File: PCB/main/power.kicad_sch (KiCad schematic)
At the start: 13 parts, among them J2 PH2 protected pack, U4 AP2112K-3.3TRG1, U6 BQ24074RGTR

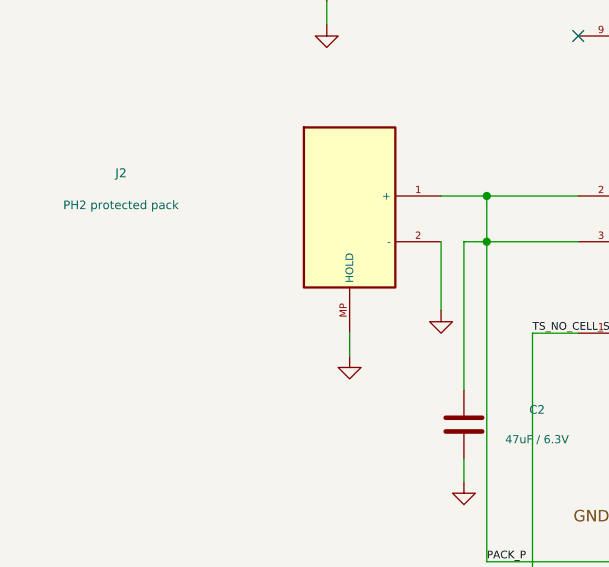
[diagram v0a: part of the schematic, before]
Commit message: Compact PCB and housing with 2.54mm PTH battery wire pads
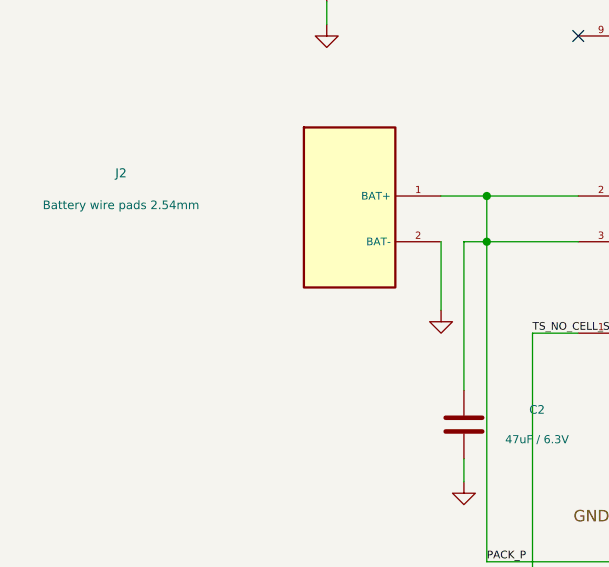
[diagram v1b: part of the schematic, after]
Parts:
- J2: value PH2 protected pack -> Battery wire pads 2.54mm; footprint smove-r2-main:JST_PH_S2B-PH-SM4-TB_1x02-1MP_P2.00mm_Horizontal -> smove-r2-main:BatteryWire_2x_PTH_P2.54mm_D1.0mm; LCSC C295747 -> (none); MPN S2B-PH-SM4-TB(LF)(SN) -> (none); now left out of the parts list
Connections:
- net GND: no longer J2.MP (HOLD)
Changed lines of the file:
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@@
     (at 50.8 77.47 0)
     (unit 1)
-    (in_bom yes)
+    (in_bom no)
     (on_board yes)
     (dnp no)
@@
         (font
           (size 1 1))))
-    (property "Value" "PH2 protected pack"
+    (property "Value" "Battery wire pads 2.54mm"
       (at 25.4 77.216 0)
       (effects
         (font
           (size 0.95 0.95))))
-    (property "Footprint" "smove-r2-main:JST_PH_S2B-PH-SM4-TB_1x02-1MP_P2.00mm_Horizontal"
+    (property "Footprint" "smove-r2-main:BatteryWire_2x_PTH_P2.54mm_D1.0mm"
       (at 50.8 77.47 0)
       (effects
@@
           (size 1 1))
         (hide yes)))
-    (property "MPN" "S2B-PH-SM4-TB(LF)(SN)"
+    (property "MPN" ""
       (at 50.8 77.47 0)
       (effects
@@
           (size 1 1))
         (hide yes)))
-    (property "LCSC" "C295747"
+    (property "LCSC" ""
       (at 50.8 77.47 0)
       (effects
@@
 )
     (pin "2"
-)
-    (pin "MP"
 )
     (instances
@@
   (symbol
     (lib_id "power:GND")
-    (at 50.8 93.98 0)
+    (at 157.48 148.59 0)
     (unit 1)
     (in_bom no)
     (on_board no)
     (dnp no)
-    (property "Reference" "#PWR10"
-      (at 50.8 86.36 0)
+    (property "Reference" "#PWR16"
+      (at 157.48 140.97 0)
       (effects
         (font
@@
         (hide yes)))
     (property "Value" "GND"
-      (at 50.8 89.916 0)
+      (at 157.48 144.526 0)
       (effects
         (font
@@
       (project "smove-r2-main"
         (path "/8e261347-838a-5848-981d-f693675e8aa0/a926f61e-132d-5af0-876e-12788077b17d"
-          (reference "#PWR10")
+          (reference "#PWR16")
           (unit 1)))))
   (symbol
     (lib_id "power:GND")
-    (at 157.48 148.59 0)
+    (at 144.78 125.73 0)
     (unit 1)
     (in_bom no)
     (on_board no)
     (dnp no)
-    (property "Reference" "#PWR16"
-      (at 157.48 140.97 0)
+    (property "Reference" "#PWR17"
+      (at 144.78 118.11 0)
       (effects
         (font
@@
         (hide yes)))
     (property "Value" "GND"
-      (at 157.48 144.526 0)
+      (at 144.78 121.666 0)
       (effects
         (font
@@
       (project "smove-r2-main"
         (path "/8e261347-838a-5848-981d-f693675e8aa0/a926f61e-132d-5af0-876e-12788077b17d"
-          (reference "#PWR16")
+          (reference "#PWR17")
           (unit 1)))))
   (symbol
     (lib_id "power:GND")
-    (at 144.78 125.73 0)
+    (at 129.54 143.51 0)
     (unit 1)
     (in_bom no)
     (on_board no)
     (dnp no)
-    (property "Reference" "#PWR17"
-      (at 144.78 118.11 0)
+    (property "Reference" "#PWR18"
+      (at 129.54 135.89 0)
       (effects
         (font
@@
         (hide yes)))
     (property "Value" "GND"
-      (at 144.78 121.666 0)
+      (at 129.54 139.446 0)
       (effects
         (font
@@
       (project "smove-r2-main"
         (path "/8e261347-838a-5848-981d-f693675e8aa0/a926f61e-132d-5af0-876e-12788077b17d"
-          (reference "#PWR17")
+          (reference "#PWR18")
           (unit 1)))))
   (symbol
     (lib_id "power:GND")
-    (at 129.54 143.51 0)
+    (at 71.12 140.97 0)
     (unit 1)
     (in_bom no)
     (on_board no)
     (dnp no)
-    (property "Reference" "#PWR18"
-      (at 129.54 135.89 0)
+    (property "Reference" "#PWR19"
+      (at 71.12 133.35 0)
       (effects
         (font
@@
         (hide yes)))
     (property "Value" "GND"
-      (at 129.54 139.446 0)
+      (at 71.12 136.906 0)
       (effects
         (font
@@
       (project "smove-r2-main"
         (path "/8e261347-838a-5848-981d-f693675e8aa0/a926f61e-132d-5af0-876e-12788077b17d"
-          (reference "#PWR18")
+          (reference "#PWR19")
           (unit 1)))))
   (symbol
     (lib_id "power:GND")
-    (at 71.12 140.97 0)
+    (at 48.26 57.15 0)
     (unit 1)
     (in_bom no)
     (on_board no)
     (dnp no)
-    (property "Reference" "#PWR19"
-      (at 71.12 133.35 0)
+    (property "Reference" "#PWR20"
+      (at 48.26 49.53 0)
       (effects
         (font
@@
         (hide yes)))
     (property "Value" "GND"
-      (at 71.12 136.906 0)
+      (at 48.26 53.086 0)
       (effects
         (font
@@
       (project "smove-r2-main"
         (path "/8e261347-838a-5848-981d-f693675e8aa0/a926f61e-132d-5af0-876e-12788077b17d"
-          (reference "#PWR19")
+          (reference "#PWR20")
           (unit 1)))))
   (symbol
     (lib_id "power:GND")
-    (at 48.26 57.15 0)
+    (at 63.5 107.95 0)
     (unit 1)
     (in_bom no)
     (on_board no)
     (dnp no)
-    (property "Reference" "#PWR20"
-      (at 48.26 49.53 0)
+    (property "Reference" "#PWR21"
+      (at 63.5 100.33 0)
       (effects
         (font
@@
         (hide yes)))
     (property "Value" "GND"
-      (at 48.26 53.086 0)
+      (at 63.5 103.886 0)
       (effects
         (font
@@
       (project "smove-r2-main"
         (path "/8e261347-838a-5848-981d-f693675e8aa0/a926f61e-132d-5af0-876e-12788077b17d"
-          (reference "#PWR20")
+          (reference "#PWR21")
           (unit 1)))))
   (symbol
     (lib_id "power:GND")
-    (at 63.5 107.95 0)
+    (at 205.74 69.85 0)
     (unit 1)
     (in_bom no)
     (on_board no)
     (dnp no)
-    (property "Reference" "#PWR21"
-      (at 63.5 100.33 0)
+    (property "Reference" "#PWR22"
+      (at 205.74 62.23 0)
       (effects
         (font
@@
         (hide yes)))
     (property "Value" "GND"
-      (at 63.5 103.886 0)
+      (at 205.74 65.786 0)
       (effects
         (font
@@
       (project "smove-r2-main"
         (path "/8e261347-838a-5848-981d-f693675e8aa0/a926f61e-132d-5af0-876e-12788077b17d"
-          (reference "#PWR21")
+          (reference "#PWR22")
           (unit 1)))))
   (symbol
     (lib_id "power:GND")
-    (at 205.74 69.85 0)
+    (at 177.8 148.59 0)
     (unit 1)
     (in_bom no)
     (on_board no)
     (dnp no)
-    (property "Reference" "#PWR22"
-      (at 205.74 62.23 0)
+    (property "Reference" "#PWR25"
+      (at 177.8 140.97 0)
       (effects
         (font
@@
         (hide yes)))
     (property "Value" "GND"
-      (at 205.74 65.786 0)
+      (at 177.8 144.526 0)
       (effects
         (font
@@
       (project "smove-r2-main"
         (path "/8e261347-838a-5848-981d-f693675e8aa0/a926f61e-132d-5af0-876e-12788077b17d"
-          (reference "#PWR22")
+          (reference "#PWR25")
           (unit 1)))))
   (symbol
     (lib_id "power:GND")
-    (at 177.8 148.59 0)
+    (at 160.02 67.31 0)
     (unit 1)
     (in_bom no)
     (on_board no)
     (dnp no)
-    (property "Reference" "#PWR25"
-      (at 177.8 140.97 0)
-      (effects
-        (font
-          (size 1 1))
-        (hide yes)))
-    (property "Value" "GND"
-      (at 177.8 144.526 0)
-      (effects
-        (font
-          (size 0.95 0.95))
-        (hide yes)))
-    (pin "1"
-)
-    (instances
-      (project "smove-r2-main"
-        (path "/8e261347-838a-5848-981d-f693675e8aa0/a926f61e-132d-5af0-876e-12788077b17d"
-          (reference "#PWR25")
-          (unit 1)))))
-  (symbol
-    (lib_id "power:GND")
-    (at 160.02 67.31 0)
-    (unit 1)
-    (in_bom no)
-    (on_board no)
-    (dnp no)
     (property "Reference" "#PWR26"
       (at 160.02 59.69 0)
@@
     (stroke
       (width 0)
-      (type default))
-)
-  (wire
-    (pts
-      (xy 50.8 91.44)
-      (xy 50.8 93.98))
-    (stroke
-      (width 0)

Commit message: Make sure it's printer friendly
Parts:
- C3: value 22uF / 10V -> 22uF / 25V; LCSC C29277 -> C45783; MPN CL21A226MPQNNNE -> CL21A226MAQNNNE
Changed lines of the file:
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@@
         (font
           (size 0.95 0.95))))
-    (property "Value" "22uF / 10V"
+    (property "Value" "22uF / 25V"
       (at 213.868 65.151 0)
       (effects
@@
           (size 1 1))
         (hide yes)))
-    (property "MPN" "CL21A226MPQNNNE"
+    (property "MPN" "CL21A226MAQNNNE"
       (at 205.74 63.5 0)
       (effects
@@
           (size 1 1))
         (hide yes)))
-    (property "LCSC" "C29277"
+    (property "LCSC" "C45783"
       (at 205.74 63.5 0)
       (effects

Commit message: Add Battery on/off switch
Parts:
- added R24: 100k, smove-r2-main:R_0402_1005Metric, symbol Device:R
- added SW1: Off-board pack toggle switch (2x wire pads 2.54mm), smove-r2-main:BatteryWire_2x_PTH_P2.54mm_D1.0mm, symbol smove-r2-main:SW1
- U4: value AP2112K-3.3TRG1 -> XC6220B331MR-G; footprint smove-r2-main:SOT-23-5 -> smove-r2-main:SOT-25_XC6220; LCSC C51118 -> C86534; MPN AP2112K-3.3TRG1 -> XC6220B331MR-G
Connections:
- net 3V3_MAIN: now also R24.1
- net PACK_P: now also SW1.1 (A); no longer J2.1 (BAT+)
- net CHG_N: now reaches U6.9 (CHG_N)
- net CHG_N: now also R24.2
- new net PACK_RAW: J2.1 (BAT+), SW1.2 (B)
- no-connect marks 4 -> 3
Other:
- note added: "SW1: hard pack cutoff in the J2 + lead (off-board toggle, >=0.5A, contacts <50 mOhm, >=6V DC)."
- note added: "U4 = XC6220B331MR-G SOT-25 (1A, ~60mV dropout @300mA). R24 pulls charger CHG_N up to 3V3_MAIN on U1 GPIO6."
- moved on the sheet: J2
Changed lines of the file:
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@@
         (font
           (size 1 1))))
-    (property "Value" "AP2112K-3.3TRG1"
+    (property "Value" "XC6220B331MR-G"
       (at 187.96 32.766 0)
       (effects
         (font
           (size 0.95 0.95))))
-    (property "Footprint" "smove-r2-main:SOT-23-5"
+    (property "Footprint" "smove-r2-main:SOT-25_XC6220"
       (at 187.96 50.8 0)
       (effects
@@
           (size 1 1))
         (hide yes)))
-    (property "MPN" "AP2112K-3.3TRG1"
+    (property "MPN" "XC6220B331MR-G"
       (at 187.96 50.8 0)
       (effects
@@
           (size 1 1))
         (hide yes)))
-    (property "LCSC" "C51118"
+    (property "LCSC" "C86534"
       (at 187.96 50.8 0)
       (effects
@@
   (symbol
     (lib_id "smove-r2-main:J2")
-    (at 50.8 77.47 0)
+    (at 50.8 87.63 0)
     (unit 1)
     (in_bom no)
@@
     (dnp no)
     (property "Reference" "J2"
-      (at 25.4 73.66 0)
+      (at 25.4 83.82 0)
       (effects
         (font
           (size 1 1))))
     (property "Value" "Battery wire pads 2.54mm"
-      (at 25.4 77.216 0)
+      (at 25.4 87.376 0)
       (effects
         (font
@@
 )
   (no_connect
-    (at 76.2 58.42)
-)
-  (no_connect
     (at 137.16 93.98)
 )
@@
   (wire
     (pts
-      (xy 60.96 76.2)
-      (xy 66.04 76.2))
-    (stroke
-      (width 0)
-      (type default))
-)
-  (wire
-    (pts
       (xy 66.04 76.2)
       (xy 76.2 76.2))
@@
   (wire
     (pts
-      (xy 60.96 81.28)
+      (xy 60.96 91.44)
       (xy 60.96 88.9))
     (stroke
@@
         (size 1.52 1.52))
       (justify left))
+)
+  (symbol
+    (lib_id "smove-r2-main:SW1")
+    (at 50.8 66.04 0)
+    (unit 1)
+    (in_bom no)
+    (on_board yes)
+    (dnp no)
+    (property "Reference" "SW1"
+      (at 44.45 55.88 0)
+      (effects
+        (font
+          (size 0.95 0.95))))
+    (property "Value" "Off-board pack toggle switch (2x wire pads 2.54mm)"
+      (at 44.45 58.42 0)
+      (effects
+        (font
+          (size 0.95 0.95))))
+    (property "Footprint" "smove-r2-main:BatteryWire_2x_PTH_P2.54mm_D1.0mm"
+      (at 50.8 66.04 0)
+      (effects
+        (font
+          (size 1 1))
+        (hide yes)))
+    (property "MPN" ""
+      (at 50.8 66.04 0)
+      (effects
+        (font
+          (size 1 1))
+        (hide yes)))
+    (property "LCSC" ""
+      (at 50.8 66.04 0)
+      (effects
+        (font
+          (size 1 1))
+        (hide yes)))
+    (pin "1"
+)
+    (pin "2"
+)
+    (instances
+      (project "smove-r2-main"
+        (path "/8e261347-838a-5848-981d-f693675e8aa0/a926f61e-132d-5af0-876e-12788077b17d"
+          (reference "SW1")
+          (unit 1)))))
+  (symbol
+    (lib_id "Device:R")
+    (at 66.04 52.07 0)
+    (unit 1)
+    (in_bom yes)
+    (on_board yes)
+    (dnp no)
+    (property "Reference" "R24"
+      (at 74.168 50.419 0)
+      (effects
+        (font
+          (size 0.95 0.95))))
+    (property "Value" "100k"
+      (at 74.168 53.721 0)
+      (effects
+        (font
+          (size 0.95 0.95))))
+    (property "Footprint" "smove-r2-main:R_0402_1005Metric"
+      (at 66.04 52.07 0)
+      (effects
+        (font
+          (size 1 1))
+        (hide yes)))
+    (property "MPN" "0402WGF1003TCE"
+      (at 66.04 52.07 0)
+      (effects
+        (font
+          (size 1 1))
+        (hide yes)))
+    (property "LCSC" "C25741"
+      (at 66.04 52.07 0)
+      (effects
+        (font
+          (size 1 1))
+        (hide yes)))
+    (pin "1"
+)
+    (pin "2"
+)
+    (instances
+      (project "smove-r2-main"
+        (path "/8e261347-838a-5848-981d-f693675e8aa0/a926f61e-132d-5af0-876e-12788077b17d"
+          (reference "R24")
+          (unit 1)))))
+  (wire
+    (pts
+      (xy 60.96 69.85)
+      (xy 60.96 86.36))
+    (stroke
+      (width 0)
+      (type default))
+)
+  (wire
+    (pts
+      (xy 60.96 64.77)
+      (xy 78.74 64.77))
+    (stroke
+      (width 0)
+      (type default))
+)
+  (wire
+    (pts
+      (xy 78.74 64.77)
+      (xy 78.74 76.2))
+    (stroke
+      (width 0)
+      (type default))
+)
+  (wire
+    (pts
+      (xy 78.74 76.2)
+      (xy 76.2 76.2))
+    (stroke
+      (width 0)
+      (type default))
+)
+  (wire
+    (pts
+      (xy 66.04 55.88)
+      (xy 66.04 58.42))
+    (stroke
+      (width 0)
+      (type default))
+)
+  (wire
+    (pts
+      (xy 66.04 48.26)
+      (xy 68.58 48.26))
+    (stroke
+      (width 0)
+      (type default))
+)
+  (wire
+    (pts
+      (xy 66.04 58.42)
+      (xy 71.12 58.42))
+    (stroke
+      (width 0)
+      (type default))
+)
+  (wire
+    (pts
+      (xy 71.12 58.42)
+      (xy 76.2 58.42))
+    (stroke
+      (width 0)
+      (type default))
+)
+  (wire
+    (pts
+      (xy 71.12 58.42)
+      (xy 71.12 55.88))
+    (stroke
+      (width 0)
+      (type default))
+)
+  (junction
+    (at 76.2 76.2)
+    (diameter 0)
+    (color 0 0 0 0)
+)
+  (junction
+    (at 71.12 58.42)
+    (diameter 0)
+    (color 0 0 0 0)
+)
+  (label "PACK_RAW"
+    (at 60.96 78.74 90)
+    (effects
+      (font
+        (size .85 .85))
+      (justify left bottom))
+)
+  (hierarchical_label "3V3_MAIN"
+    (shape output)
+    (at 68.58 48.26 0)
+    (effects
+      (font
+        (size 1.27 1.27))
+      (justify left))
+)
+  (hierarchical_label "CHG_N"
+    (shape output)
+    (at 71.12 55.88 90)
+    (effects
+      (font
+        (size 1.27 1.27))
+      (justify left))
+)
+  (text "SW1: hard pack cutoff in the J2 + lead (off-board toggle, >=0.5A, contacts <50 mOhm, >=6V DC)."
+    (at 25.4 165.1 0)
+    (effects
+      (font
+        (size 1 1))
+      (justify left))
+)
+  (text "U4 = XC6220B331MR-G SOT-25 (1A, ~60mV dropout @300mA). R24 pulls charger CHG_N up to 3V3_MAIN on U1 GPIO6."
+    (at 25.4 168.91 0)
+    (effects
+      (font
+        (size 1 1))
+      (justify left))
 ))

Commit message: power: hardwire BQ24074 EN1 high to select USB500 input limit
- Remove EN1 (U6.6) tie to GND; add R25 (100k 0402, 0402WGF1003TCE) from EN1 to SYS (U6 OUT rail)
- CE_N/EN2/VSS/EP remain grounded; ISET/ILIM/TS unchanged
- Update stale sheet annotations (USB500 ~500 mA; no source/CC awareness)
- Schematic-only ECO: layout/routing intentionally not updated
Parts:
- added R25: 100k, smove-r2-main:R_0402_1005Metric, symbol Device:R
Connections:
- net GND: no longer U6.6 (EN1)
- net SYS: now also R25.2
- new net: R25.1, U6.6 (EN1)
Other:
- note added: "NO cell sensing: TS 10k bias. TMR / ITERM open; CE / EN2 grounded; EN1 pulled up to SYS = USB500. No source/CC awareness."
- note added: "USB500 input-current limit ~500mA (450mA guaranteed-min): EN1 pulled up to SYS. Protected 4.2V pack only. No automatic cell-temperature sensing."
- note removed: "NO cell sensing: TS 10k bias. TMR / ITERM open; CE / EN1 / EN2 grounded."
- note removed: "USB100 fixed (90mA guaranteed-min input). Protected 4.2V pack only. No automatic cell-temperature sensing."
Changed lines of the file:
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@@
-  (wire
-    (pts
-      (xy 106.68 106.68)
-      (xy 106.68 111.76))
-    (stroke
-      (width 0)
-      (type default))
-)
   (wire
     (pts
@@
   (wire
     (pts
+      (xy 106.68 106.68)
+      (xy 106.68 107.95))
+    (stroke
+      (width 0)
+      (type default))
+)
+  (wire
+    (pts
+      (xy 106.68 107.95)
+      (xy 134.62 107.95))
+    (stroke
+      (width 0)
+      (type default))
+)
+  (wire
+    (pts
+      (xy 134.62 115.57)
+      (xy 137.16 115.57))
+    (stroke
+      (width 0)
+      (type default))
+)
+  (wire
+    (pts
       (xy 86.36 111.76)
       (xy 96.52 111.76))
@@
 )
   (junction
-    (at 106.68 111.76)
-    (diameter 0)
-    (color 0 0 0 0)
-)
-  (junction
     (at 116.84 111.76)
     (diameter 0)
@@
       (justify left bottom))
 )
-  (text "USB100 fixed (90mA guaranteed-min input). Protected 4.2V pack only. No automatic cell-temperature sensing."
+  (text "USB500 input-current limit ~500mA (450mA guaranteed-min): EN1 pulled up to SYS. Protected 4.2V pack only. No automatic cell-temperature sensing."
     (at 25.4 24.13 0)
     (effects
@@
       (justify left))
 )
-  (text "NO cell sensing: TS 10k bias. TMR / ITERM open; CE / EN1 / EN2 grounded."
+  (text "NO cell sensing: TS 10k bias. TMR / ITERM open; CE / EN2 grounded; EN1 pulled up to SYS = USB500. No source/CC awareness."
     (at 25.4 170.18 0)
     (effects
@@
         (size 1 1))
       (justify left))
+)
+  (symbol
+    (lib_id "Device:R")
+    (at 134.62 111.76 0)
+    (unit 1)
+    (in_bom yes)
+    (on_board yes)
+    (dnp no)
+    (property "Reference" "R25"
+      (at 142.748 110.109 0)
+      (effects
+        (font
+          (size .95 .95))))
+    (property "Value" "100k"
+      (at 142.748 113.411 0)
+      (effects
+        (font
+          (size .9 .9))))
+    (property "Footprint" "smove-r2-main:R_0402_1005Metric"
+      (at 134.62 111.76 0)
+      (effects
+        (font
+          (size 1 1))
+        (hide yes)))
+    (property "MPN" "0402WGF1003TCE"
+      (at 134.62 111.76 0)
+      (effects
+        (font
+          (size 1 1))
+        (hide yes)))
+    (property "LCSC" "C25741"
+      (at 134.62 111.76 0)
+      (effects
+        (font
+          (size 1 1))
+        (hide yes)))
+    (pin "1"
+)
+    (pin "2"
+)
+    (instances
+      (project "smove-r2-main"
+        (path "/8e261347-838a-5848-981d-f693675e8aa0/a926f61e-132d-5af0-876e-12788077b17d"
+          (reference "R25")
+          (unit 1)))))
+  (label "SYS"
+    (at 137.16 115.57 0)
+    (effects
+      (font
+        (size .85 .85))
+      (justify left bottom))
 ))
